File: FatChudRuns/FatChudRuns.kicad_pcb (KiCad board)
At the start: 2 copper layers, 48 parts, among them J1 RJ45_Pulse_JXD6-0001NL, J2 Conn_02x20_Odd_Even, J3 FTSH-107-01-L-DV-K-P, U1 STM32F107RBTx, U2 DP83848I

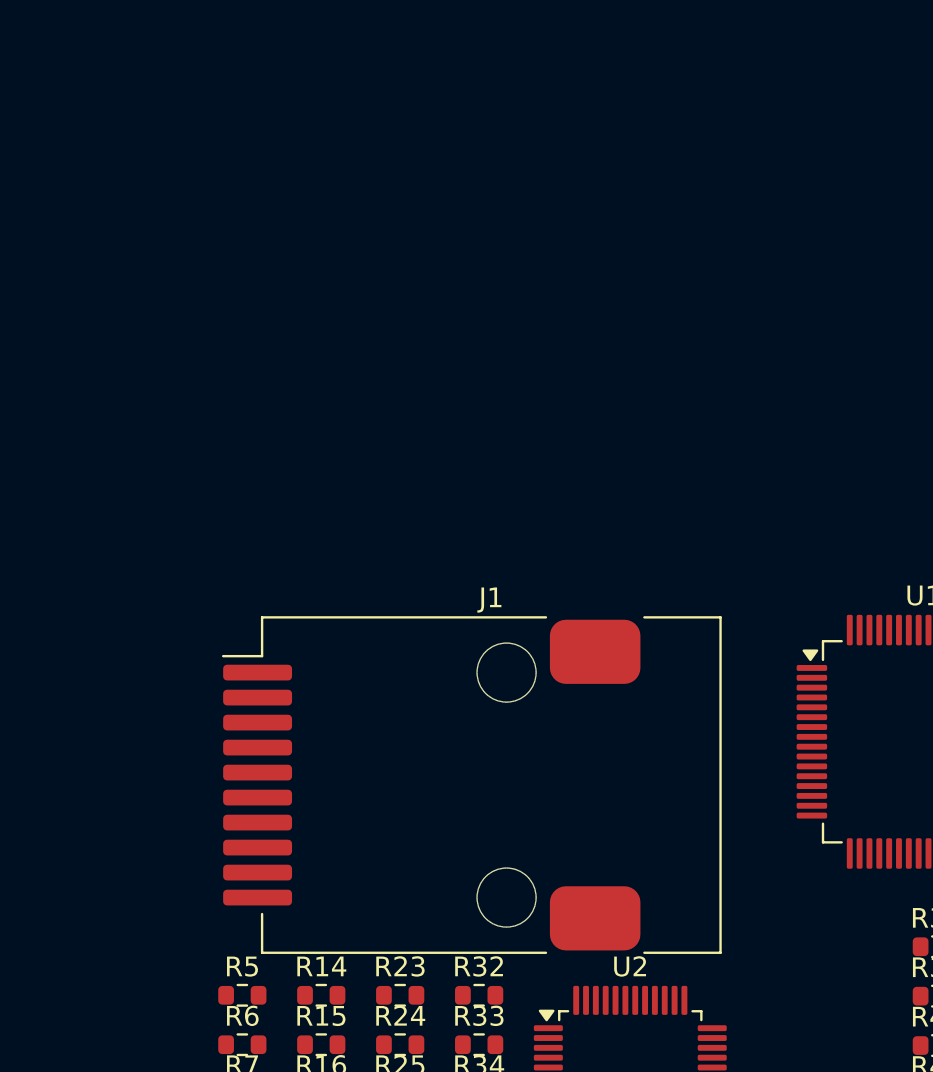
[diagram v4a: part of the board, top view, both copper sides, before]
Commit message: added caps and diode footprints, all caps now non-polarized ceramic caps
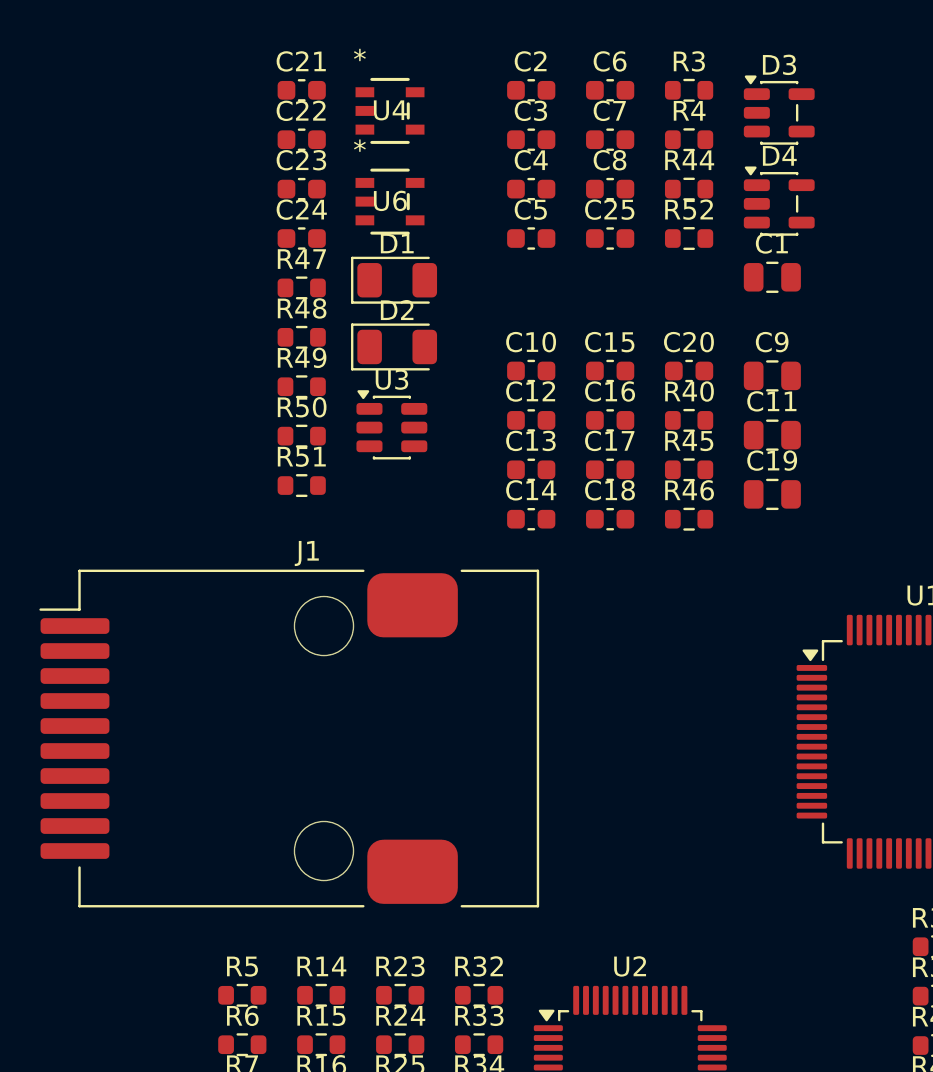
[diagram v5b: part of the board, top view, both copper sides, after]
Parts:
- added C1: 10uF, Capacitor_SMD:C_0805_2012Metric, F.Cu at (-27.5, 41.2)
- added C10: 100nF, Capacitor_SMD:C_0603_1608Metric, F.Cu at (-39.8, 45.9)
- added C11: 10uF, Capacitor_SMD:C_0805_2012Metric, F.Cu at (-27.5, 49.2)
- added C12: 100nF, Capacitor_SMD:C_0603_1608Metric, F.Cu at (-39.8, 48.5)
- added C13: 100nF, Capacitor_SMD:C_0603_1608Metric, F.Cu at (-39.8, 51.0)
- added C14: 100nF, Capacitor_SMD:C_0603_1608Metric, F.Cu at (-39.8, 53.5)
- added C15: 100nF, Capacitor_SMD:C_0603_1608Metric, F.Cu at (-35.8, 45.9)
- added C16: 100nF, Capacitor_SMD:C_0603_1608Metric, F.Cu at (-35.8, 48.5)
- added C17: 100nF, Capacitor_SMD:C_0603_1608Metric, F.Cu at (-35.8, 51.0)
- added C18: 100nF, Capacitor_SMD:C_0603_1608Metric, F.Cu at (-35.8, 53.5)
- added C19: 10uF, Capacitor_SMD:C_0805_2012Metric, F.Cu at (-27.5, 52.2)
- added C2: 100nF, Capacitor_SMD:C_0603_1608Metric, F.Cu at (-39.8, 31.7)
- added C20: 100nF, Capacitor_SMD:C_0603_1608Metric, F.Cu at (-31.7, 45.9)
- added C21: 1uF, Capacitor_SMD:C_0603_1608Metric, F.Cu at (-51.4, 31.7)
- added C22: 1uF, Capacitor_SMD:C_0603_1608Metric, F.Cu at (-51.4, 34.2)
- added C23: 1uF, Capacitor_SMD:C_0603_1608Metric, F.Cu at (-51.4, 36.7)
- added C24: 1uF, Capacitor_SMD:C_0603_1608Metric, F.Cu at (-51.4, 39.2)
- added C25: 100nF, Capacitor_SMD:C_0603_1608Metric, F.Cu at (-35.8, 39.2)
- added C3: 100nF, Capacitor_SMD:C_0603_1608Metric, F.Cu at (-39.8, 34.2)
- added C4: 100nF, Capacitor_SMD:C_0603_1608Metric, F.Cu at (-39.8, 36.7)
- added C5: 100nF, Capacitor_SMD:C_0603_1608Metric, F.Cu at (-39.8, 39.2)
- added C6: 100nF, Capacitor_SMD:C_0603_1608Metric, F.Cu at (-35.8, 31.7)
- added C7: 1uF, Capacitor_SMD:C_0603_1608Metric, F.Cu at (-35.8, 34.2)
- added C8: 100nF, Capacitor_SMD:C_0603_1608Metric, F.Cu at (-35.8, 36.7)
- added C9: 10uF, Capacitor_SMD:C_0805_2012Metric, F.Cu at (-27.5, 46.2)
- added D1: IR26-21C_L110_TR8, LED_SMD:LED_1206_3216Metric, F.Cu at (-46.6, 41.3)
- added D2: IR26-21C_L110_TR8, LED_SMD:LED_1206_3216Metric, F.Cu at (-46.6, 44.7)
- added D3: ESDA6V1SC5, Package_TO_SOT_SMD:SOT-23-5, F.Cu at (-27.2, 32.8)
- added D4: ESDA6V1SC5, Package_TO_SOT_SMD:SOT-23-5, F.Cu at (-27.2, 37.5)
- added R3: 4.7k, Resistor_SMD:R_0603_1608Metric, F.Cu at (-31.7, 31.7)
- added R4: 4.7k, Resistor_SMD:R_0603_1608Metric, F.Cu at (-31.7, 34.2)
- added R40: 220, Resistor_SMD:R_0603_1608Metric, F.Cu at (-31.7, 48.5)
- added R44: 100, Resistor_SMD:R_0603_1608Metric, F.Cu at (-31.7, 36.7)
- added R45: 0, Resistor_SMD:R_0603_1608Metric, F.Cu at (-31.7, 51.0)
- added R46: 0, Resistor_SMD:R_0603_1608Metric, F.Cu at (-31.7, 53.5)
- added R47: 5.1k, Resistor_SMD:R_0603_1608Metric, F.Cu at (-51.4, 41.7)
- added R48: 5.1k, Resistor_SMD:R_0603_1608Metric, F.Cu at (-51.4, 44.2)
- added R49: 4.7k, Resistor_SMD:R_0603_1608Metric, F.Cu at (-51.4, 46.7)
- added R50: 220, Resistor_SMD:R_0603_1608Metric, F.Cu at (-51.4, 49.3)
- added R51: 220, Resistor_SMD:R_0603_1608Metric, F.Cu at (-51.4, 51.8)
- added R52: 220, Resistor_SMD:R_0603_1608Metric, F.Cu at (-31.7, 39.2)
- added U3: USBLC6-2SC6, Package_TO_SOT_SMD:SOT-23-6, F.Cu at (-46.8, 48.8)
- added U4: ST730M33R, SOT_30M33R_STM:SOT_30M33R_STM, F.Cu at (-46.9, 32.7)
- added U6: ST730M33R, SOT_30M33R_STM:SOT_30M33R_STM, F.Cu at (-46.9, 37.3)
- J2: value Conn_02x20_Odd_Even -> Z-21320110021001
- R39: value 110 -> 220
- U1: value STM32F107RBTx -> STM32F107RBT6
- moved J1 9.57 mm to (-51.1, 64.6)
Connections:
- net Net-(U2-RX_ER/MDIX_EN) renamed /ETH_PHY/MDIX_EN
- net VP3V3A renamed +3.3VA
- J1 pad 3: VP3V3 -> +3.3V
- J1 pad 8: VP3V3 -> +3.3V
- J2 pad 1: unconnected-(J2-Pin_1-Pad1) -> +3.3V
- J2 pad 10: unconnected-(J2-Pin_10-Pad10) -> /MCU/PA4
- J2 pad 11: unconnected-(J2-Pin_11-Pad11) -> /MCU/PC0
- J2 pad 12: unconnected-(J2-Pin_12-Pad12) -> /MCU/PA5
- J2 pad 13: unconnected-(J2-Pin_13-Pad13) -> /MCU/PC2
- J2 pad 14: unconnected-(J2-Pin_14-Pad14) -> /MCU/PA6
- J2 pad 15: unconnected-(J2-Pin_15-Pad15) -> /MCU/PC3
- J2 pad 16: unconnected-(J2-Pin_16-Pad16) -> /MCU/PA9
- J2 pad 17: unconnected-(J2-Pin_17-Pad17) -> /MCU/PC6
- J2 pad 18: unconnected-(J2-Pin_18-Pad18) -> /MCU/PA10
- J2 pad 19: unconnected-(J2-Pin_19-Pad19) -> /MCU/PC7
- J2 pad 2: unconnected-(J2-Pin_2-Pad2) -> +3.3V
- J2 pad 20: unconnected-(J2-Pin_20-Pad20) -> /MCU/PB0
- J2 pad 21: unconnected-(J2-Pin_21-Pad21) -> /MCU/PC8
- J2 pad 22: unconnected-(J2-Pin_22-Pad22) -> /MCU/PB1
- J2 pad 23: unconnected-(J2-Pin_23-Pad23) -> /MCU/PC9
- J2 pad 24: unconnected-(J2-Pin_24-Pad24) -> /MCU/PB2
- J2 pad 25: unconnected-(J2-Pin_25-Pad25) -> /MCU/PC10
- J2 pad 26: unconnected-(J2-Pin_26-Pad26) -> /MCU/PB5
- J2 pad 27: unconnected-(J2-Pin_27-Pad27) -> /MCU/PC11
- J2 pad 28: unconnected-(J2-Pin_28-Pad28) -> /MCU/PB8
- J2 pad 29: unconnected-(J2-Pin_29-Pad29) -> /MCU/PC12
- J2 pad 3: unconnected-(J2-Pin_3-Pad3) -> +3.3V
- J2 pad 30: unconnected-(J2-Pin_30-Pad30) -> /MCU/PB9
- J2 pad 31: unconnected-(J2-Pin_31-Pad31) -> /MCU/PC13
- J2 pad 32: unconnected-(J2-Pin_32-Pad32) -> /MCU/PB10
- J2 pad 33: unconnected-(J2-Pin_33-Pad33) -> /MCU/PC14
- J2 pad 34: unconnected-(J2-Pin_34-Pad34) -> /MCU/PB14
- J2 pad 35: unconnected-(J2-Pin_35-Pad35) -> /MCU/PC15
- J2 pad 36: unconnected-(J2-Pin_36-Pad36) -> /MCU/PB15
- J2 pad 37: unconnected-(J2-Pin_37-Pad37) -> GND
- J2 pad 38: unconnected-(J2-Pin_38-Pad38) -> GND
- J2 pad 39: unconnected-(J2-Pin_39-Pad39) -> GND
- J2 pad 4: unconnected-(J2-Pin_4-Pad4) -> +3.3V
- J2 pad 40: unconnected-(J2-Pin_40-Pad40) -> GND
- J2 pad 5: unconnected-(J2-Pin_5-Pad5) -> /MCU/PD0
- J2 pad 6: unconnected-(J2-Pin_6-Pad6) -> /MCU/PA0
- J2 pad 7: unconnected-(J2-Pin_7-Pad7) -> /MCU/PD1
- J2 pad 8: unconnected-(J2-Pin_8-Pad8) -> /MCU/PA3
- J2 pad 9: unconnected-(J2-Pin_9-Pad9) -> /MCU/PD2
- J3 pad 10: unconnected-(J3-Pin_10-Pad10) -> /MCU/T_JTDI
- J3 pad 11: unconnected-(J3-Pin_11-Pad11) -> /MCU/GND_DETECT
- J3 pad 12: unconnected-(J3-Pin_12-Pad12) -> /MCU/T_NRST
- J3 pad 13: unconnected-(J3-Pin_13-Pad13) -> /MCU/T_VCP_RX
- J3 pad 14: unconnected-(J3-Pin_14-Pad14) -> /MCU/T_VCP_TX
- J3 pad 3: unconnected-(J3-Pin_3-Pad3) -> +3.3V
- J3 pad 4: unconnected-(J3-Pin_4-Pad4) -> /MCU/T_SWDIO
- J3 pad 5: unconnected-(J3-Pin_5-Pad5) -> GND
- J3 pad 6: unconnected-(J3-Pin_6-Pad6) -> /MCU/T_SWCLK
- J3 pad 7: unconnected-(J3-Pin_7-Pad7) -> GND
- J3 pad 8: unconnected-(J3-Pin_8-Pad8) -> /MCU/T_SWO
- R1 pad 1: VP3V3 -> +3.3V
- R10 pad 1: VP3V3 -> +3.3V
- R11 pad 1: VP3V3 -> +3.3V
- R13 pad 1: VP3V3 -> +3.3V
- R17 pad 1: VP3V3 -> +3.3V
- R18 pad 1: VP3V3 -> +3.3V
- R19 pad 1: VP3V3 -> +3.3V
- R2 pad 1: VP3V3 -> +3.3V
- R21 pad 1: VP3V3 -> +3.3V
- R27 pad 1: VP3V3 -> +3.3V
- R29 pad 1: VP3V3 -> +3.3V
- R31 pad 1: VP3V3 -> +3.3V
- R32 pad 2: VP3V3 -> +3.3V
- R33 pad 1: VP3V3 -> +3.3V
- R34 pad 2: VP3V3 -> +3.3V
- R38 pad 1: VP3V3 -> +3.3V
- R39 pad 1: VP3V3 -> +3.3V
- R41 pad 1: VP3V3 -> +3.3V
- R42 pad 1: VP3V3 -> +3.3V
- R43 pad 1: VP3V3 -> +3.3V
- R5 pad 1: VP3V3 -> +3.3V
- R7 pad 1: VP3V3 -> +3.3V
- U1 pad 1: VP3V3 -> +3.3V
- U1 pad 19: VP3V3 -> +3.3V
- U1 pad 32: VP3V3 -> +3.3V
- U1 pad 44: /MCU/PA11 -> USB_D-
- U1 pad 45: /MCU/PA12 -> USB_D+
- U1 pad 46: /MCU/PA13 -> /MCU/T_SWDIO
- U1 pad 48: VP3V3 -> +3.3V
- U1 pad 49: /MCU/PA14 -> /MCU/T_SWCLK
- U1 pad 50: /MCU/PA15 -> /MCU/T_JTDI
- U1 pad 55: /MCU/PB3 -> /MCU/T_SWO
- U1 pad 56: /MCU/PB4 -> /MCU/T_NRST
- U1 pad 58: /MCU/PB6 -> /MCU/T_VCP_TX
- U1 pad 59: /MCU/PB7 -> /MCU/T_VCP_RX
- U1 pad 64: VP3V3 -> +3.3V

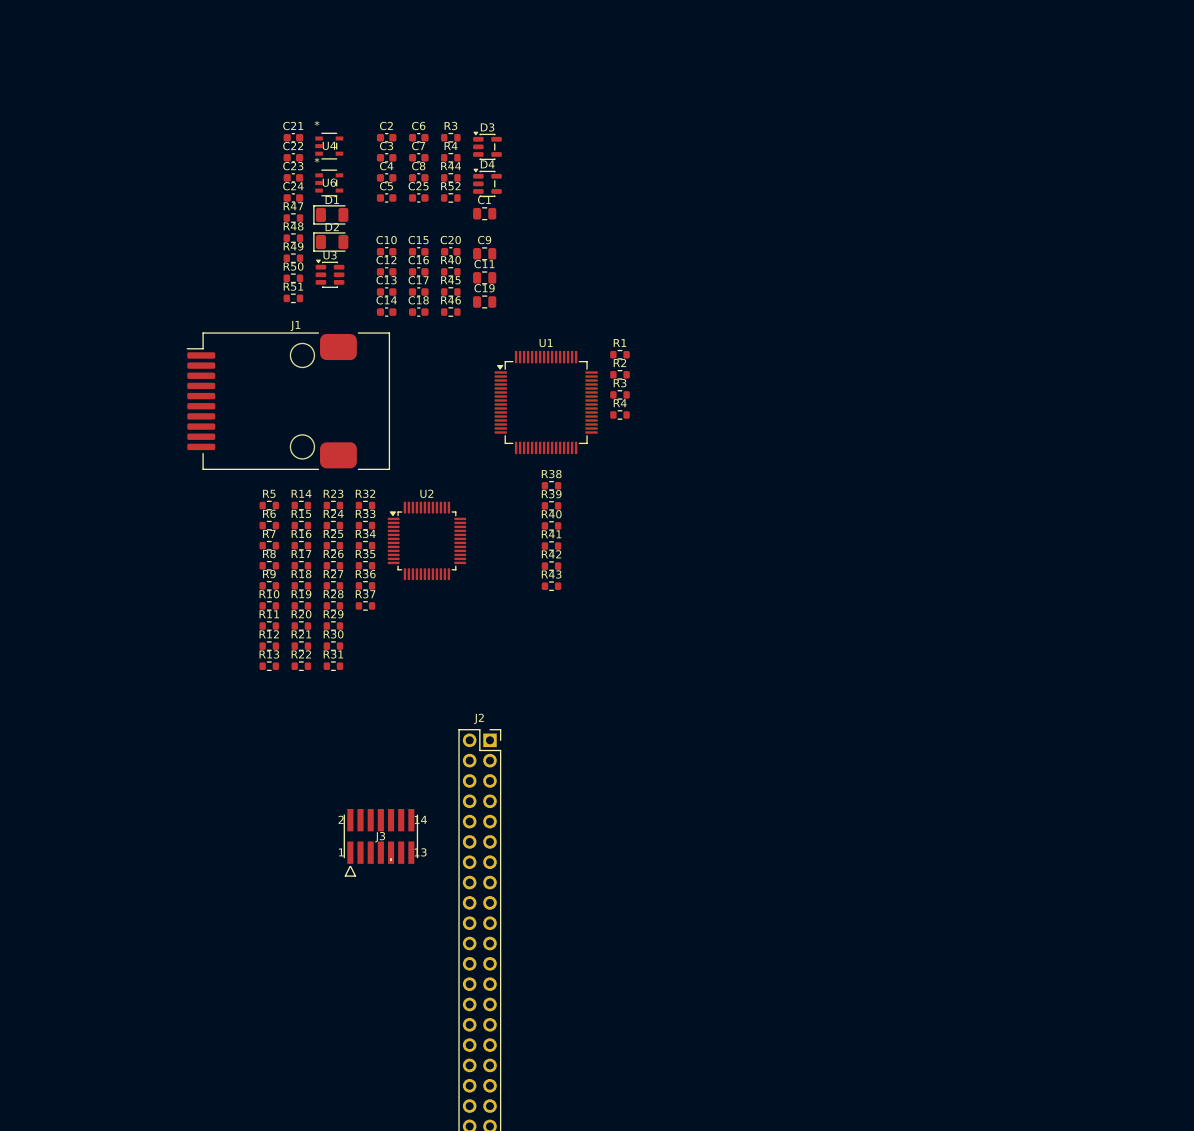
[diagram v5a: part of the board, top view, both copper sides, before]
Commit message: added footprint for switches and button - ready for layout
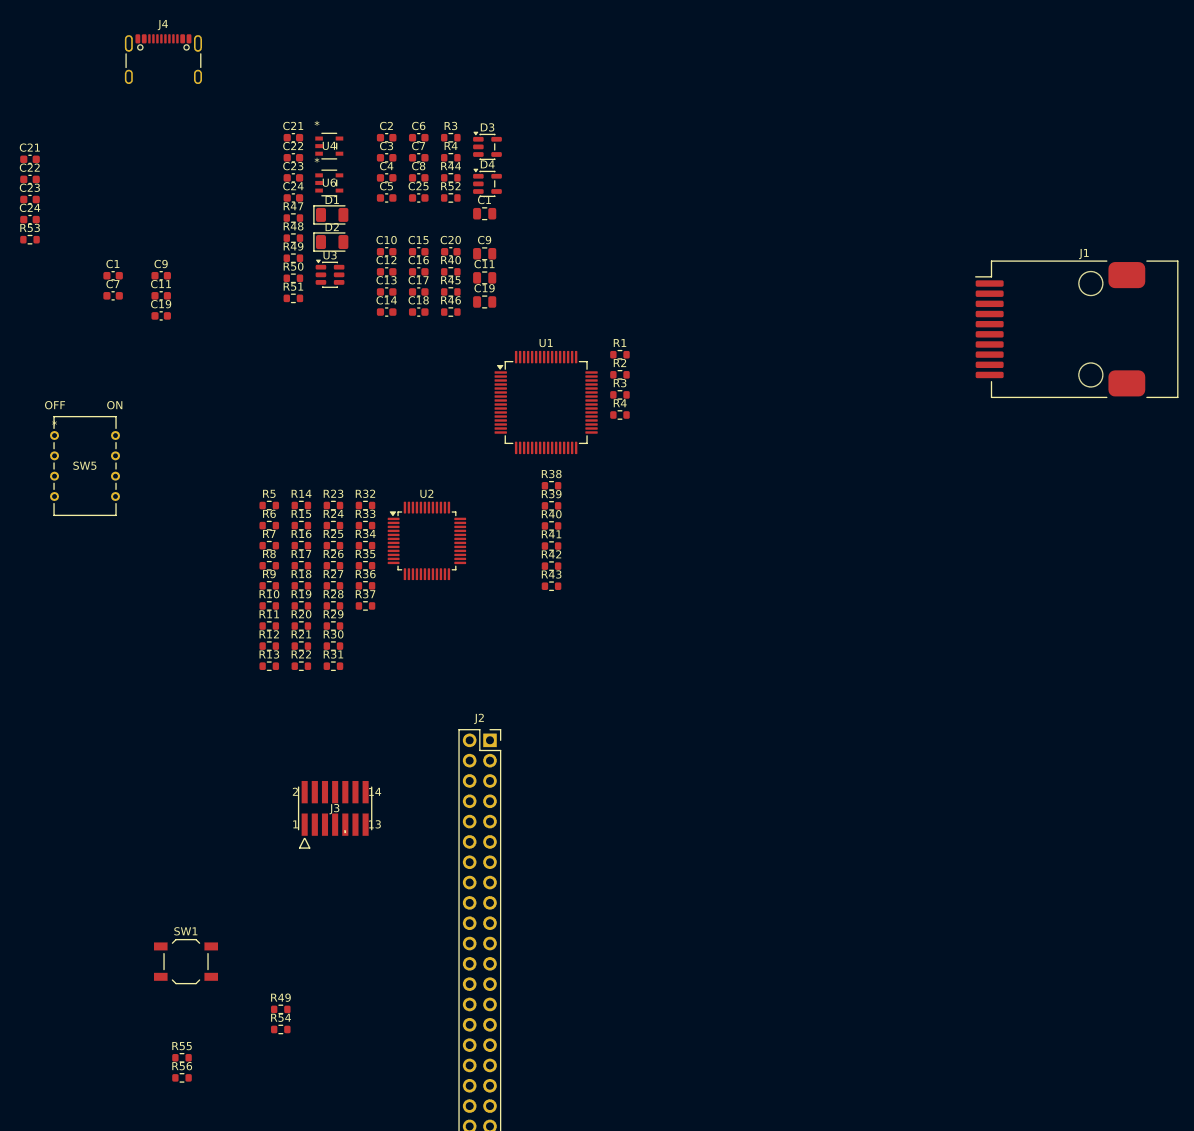
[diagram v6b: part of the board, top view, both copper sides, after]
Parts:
- added C1: 10uF, Capacitor_SMD:C_0603_1608Metric, F.Cu at (-74.0, 48.9)
- added C11: 10uF, Capacitor_SMD:C_0603_1608Metric, F.Cu at (-67.9, 51.4)
- added C19: 10uF, Capacitor_SMD:C_0603_1608Metric, F.Cu at (-67.9, 54.0)
- added C21: 1uF, Capacitor_SMD:C_0603_1608Metric, F.Cu at (-84.3, 34.4)
- added C22: 1uF, Capacitor_SMD:C_0603_1608Metric, F.Cu at (-84.3, 36.9)
- added C23: 1uF, Capacitor_SMD:C_0603_1608Metric, F.Cu at (-84.3, 39.4)
- added C24: 1uF, Capacitor_SMD:C_0603_1608Metric, F.Cu at (-84.3, 41.9)
- added C7: 1uF, Capacitor_SMD:C_0603_1608Metric, F.Cu at (-74.0, 51.4)
- added C9: 10uF, Capacitor_SMD:C_0603_1608Metric, F.Cu at (-67.9, 48.9)
- added J4: TYPE-C-31-M-12, Connector_USB:USB_C_Receptacle_GCT_USB4105-xx-A_16P_TopMnt_Horizontal, F.Cu at (-67.7, 23.0)
- added R49: 0, Resistor_SMD:R_0603_1608Metric, F.Cu at (-53.0, 140.6)
- added R53: 4.7k, Resistor_SMD:R_0603_1608Metric, F.Cu at (-84.3, 44.4)
- added R54: 0, Resistor_SMD:R_0603_1608Metric, F.Cu at (-53.0, 143.2)
- added R55: 0, Resistor_SMD:R_0603_1608Metric, F.Cu at (-65.3, 146.7)
- added R56: 0, Resistor_SMD:R_0603_1608Metric, F.Cu at (-65.3, 149.2)
- added SW1: TS-1187A-B-A-B, Button_Switch_SMD:SW_SPST_TL3342, F.Cu at (-64.8, 134.7)
- added SW5: 1825360-3, 1825360_3:SWDIP8_300X185P100, F.Cu at (-81.3, 68.9)
- moved J1 99.0 mm to (47.5, 55.6)
- moved J3 6.70 mm to (-46.2, 115.5)
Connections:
- R2 pad 2: Net-(U1-BOOT0) -> /MCU/BOOT0
- R3 pad 1: Net-(U1-BOOT0) -> /MCU/BOOT0
- U1 pad 58: /MCU/T_VCP_TX -> Net-(U1-PB6)
- U1 pad 59: /MCU/T_VCP_RX -> Net-(U1-PB7)
- U1 pad 60: Net-(U1-BOOT0) -> /MCU/BOOT0
- U3 pad 4: USB_D+ -> Net-(R54-Pad1)
- U3 pad 6: USB_D- -> Net-(R49-Pad1)

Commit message: setup stackup and constraints
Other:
- copper layers 2 -> 4
- rule pad_to_mask_clearance: 0 -> 0.15
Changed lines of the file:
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@@
 	(generator_version "9.0")
 	(general
-		(thickness 1.6)
+		(thickness 1.5842)
 		(legacy_teardrops no)
 	)
@@
 	(layers
 		(0 "F.Cu" signal)
+		(4 "In1.Cu" power)
+		(6 "In2.Cu" power)
 		(2 "B.Cu" signal)
 		(9 "F.Adhes" user "F.Adhesive")
@@
 			)
 			(layer "dielectric 1"
+				(type "prepreg")
+				(thickness 0.0994)
+				(material "FR4")
+				(epsilon_r 4.1)
+				(loss_tangent 0.02)
+			)
+			(layer "In1.Cu"
+				(type "copper")
+				(thickness 0.0152)
+			)
+			(layer "dielectric 2"
 				(type "core")
-				(thickness 1.51)
+				(thickness 1.265)
 				(material "FR4")
-				(epsilon_r 4.5)
+				(epsilon_r 4.6)
+				(loss_tangent 0.02)
+			)
+			(layer "In2.Cu"
+				(type "copper")
+				(thickness 0.0152)
+			)
+			(layer "dielectric 3"
+				(type "prepreg")
+				(thickness 0.0994)
+				(material "FR4")
+				(epsilon_r 4.1)
 				(loss_tangent 0.02)
 			)
@@
 			)
 			(copper_finish "None")
-			(dielectric_constraints no)
+			(dielectric_constraints yes)
 		)
-		(pad_to_mask_clearance 0)
+		(pad_to_mask_clearance 0.15)
+		(solder_mask_min_width 0.25)
 		(allow_soldermask_bridges_in_footprints no)
 		(tenting front back)

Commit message: added 4pF caps and Rext to XTAL, initial placement of PCB, added board outline and gnd plane
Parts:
- added C26: ~, Capacitor_SMD:C_0603_1608Metric, F.Cu at (95.0, 156.1)
- added C28: ~, Capacitor_SMD:C_0603_1608Metric, F.Cu at (95.0, 158.6)
- added Y2: ABM8G-25.000MHZ-B4Y-T, Crystal:Crystal_SMD_Abracon_ABM8AIG-4Pin_3.2x2.5mm, F.Cu at (201.3, 116.1)
- moved SW5 281.3 mm to (191.4, 137.9), turned to 90 degrees
- moved J3 258.2 mm to (211.7, 127.5)
- moved J4 253.0 mm to (168.4, 114.0), turned to -90 degrees
- moved U2 250.8 mm to (214.1, 113.5), turned to 90 degrees
- moved SW1 243.6 mm to (178.6, 127.4), turned to 180 degrees
- moved U1 213.3 mm to (187.7, 114.0), turned to 180 degrees
- moved J2 209.9 mm to (182.8, 95.7), turned to 90 degrees
- moved J1 199.1 mm to (237.5, 115.2)
- moved C1 188.6 mm to (95.9, 130.8)
- moved C1 188.6 mm to (142.3, 123.1)
- moved C10 188.6 mm to (130.1, 127.8)
- moved C11 188.6 mm to (101.9, 133.3)
- moved C11 188.6 mm to (142.3, 131.1)
- moved C12 188.6 mm to (130.1, 130.4)
- moved C13 188.6 mm to (130.1, 132.9)
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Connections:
- net /ETH_PHY/RD_N renamed /ETH_PHY/ETH_RD-
- net /ETH_PHY/RD_P renamed /ETH_PHY/ETH_RD+
- net /ETH_PHY/TD_N renamed /ETH_PHY/ETH_TD-
- net /ETH_PHY/TD_P renamed /ETH_PHY/ETH_TD+
- J2 pad 5: /MCU/PD0 -> +3.3V
- J2 pad 7: /MCU/PD1 -> +3.3V
- R53 pad 2: /POWER/LDO_EN -> LDO_EN
- SW5 pad 8: /MCU/LDO_EN -> LDO_EN
- U1 pad 5: /MCU/PD0 -> /MCU/OSC_IN
- U1 pad 6: /MCU/PD1 -> /MCU/OSC_OUT
- U4 pad 5: /POWER/LDO_EN -> LDO_EN
- U6 pad 5: /POWER/LDO_EN -> LDO_EN
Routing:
- net /ETH_PHY/ETH_TD+: track 0.00 -> 7.79 mm
- net /ETH_PHY/ETH_TD-: track 0.00 -> 7.79 mm
- net /ETH_PHY/ETH_RD+: track 0.00 -> 7.75 mm
- net /ETH_PHY/ETH_RD-: track 0.00 -> 7.75 mm
- net GND: track 0.00 -> 1.84 mm, vias 0 -> 1
- added copper zone on In1.Cu, net GND
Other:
- board outline added: 86.9 x 54.9 mm
- board text added: "0"
- board text added: "0 mils"
- board text added: "0.02"
- board text added: "0.6 mils"
- board text added: "1"
- board text added: "1.2 mils"
- board text added: "1.38 mils"
- board text added: "3.8"
- board text added: "3.91 mils"
- board text added: "4.1"
- board text added: "4.6"
- board text added: "49.8 mils"
- board text added: "B.Cu"
- board text added: "B.Mask"
- board text added: "B.Paste"
- board text added: "B.Silkscreen"
- board text added: "Bottom Silk Screen"
- board text added: "Bottom Solder Mask"
- board text added: "Bottom Solder Paste"
- board text added: "Color"
- board text added: "Dielectric 1"
- board text added: "Dielectric 2"
- board text added: "Dielectric 3"
- board text added: "Epsilon R"
- board text added: "F.Cu"
- board text added: "F.Mask"
- board text added: "F.Paste"
- board text added: "F.Silkscreen"
- board text added: "FR4"
- board text added: "Green"
- board text added: "In1.Cu"
- board text added: "In2.Cu"
- board text added: "Layer Name"
- board text added: "Loss Tangent"
- board text added: "Material"
- board text added: "Not specified"
- board text added: "Thickness (mils)"
- board text added: "Top Silk Screen"
- board text added: "Top Solder Mask"
- board text added: "Top Solder Paste"
- board text added: "Type"
- board text added: "copper"
- board text added: "core"
- board text added: "prepreg"
